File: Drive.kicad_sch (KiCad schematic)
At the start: 11 parts, among them Q1 EPC23104, U2 ACS711xEXLT-15AB

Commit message: Getting ready for fab
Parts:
- added C38, C39, C40, C41: 100n, 100V, 0603, X7R, Capacitor_SMD:C_0603_1608Metric, symbol Device:C
- added C54, C55, C56: 1u, 100V, 0805, X7R, Capacitor_SMD:C_0805_2012Metric, symbol Device:C
- C14: DigiKey (none) -> 490-GRM155Z71A105KE01JCT-ND
- C15, C16, C19: DigiKey (none) -> 490-10700-1-ND
- C18: DigiKey (none) -> 490-4762-1-ND
- R4, R5: DigiKey (none) -> 311-4.7JRCT-ND
- U2: LCSC (none) -> C150824
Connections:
- net GND: now also C38.2, C39.2, C40.2, C41.2, C54.2, C55.2, C56.2
- net Vdrive: now also C38.1, C39.1, C40.1, C41.1, C54.1, C55.1, C56.1

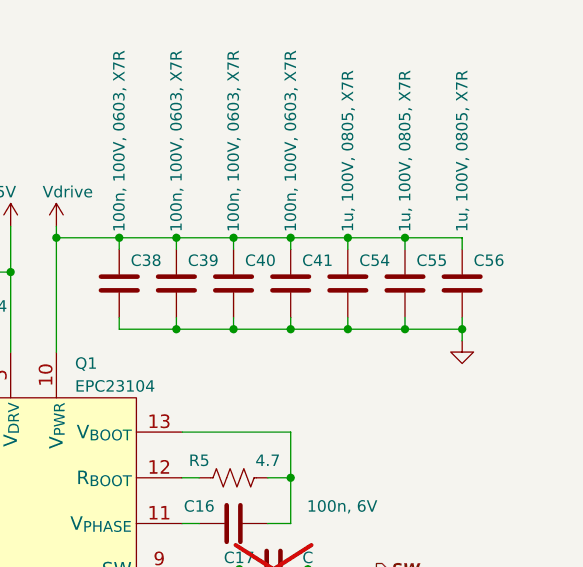
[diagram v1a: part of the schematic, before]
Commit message: Single-sided component placement
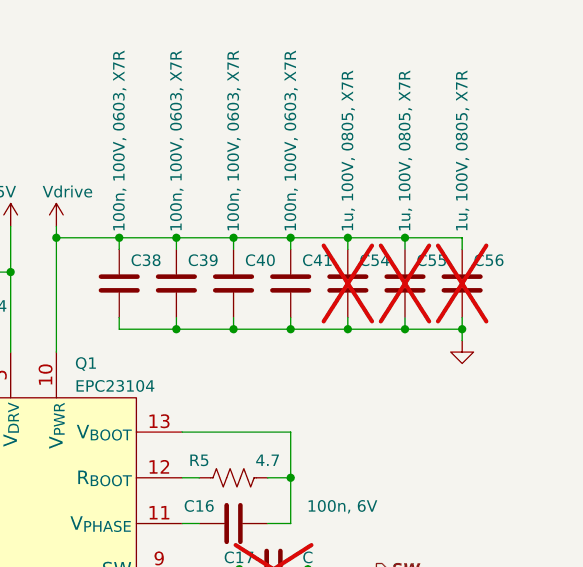
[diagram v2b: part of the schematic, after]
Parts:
- C54, C55, C56: now not fitted
- TP1: now left out of the parts list
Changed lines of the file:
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@@
   )
   (symbol (lib_id "Device:C") (at 168.275 63.5 0) (unit 1)
-    (in_bom yes) (on_board yes) (dnp no)
+    (in_bom yes) (on_board yes) (dnp yes)
     (property "Reference" "C55" (at 169.545 60.96 0)
       (effects (font (size 1.27 1.27)) (justify left))
@@
   )
   (symbol (lib_id "Device:C") (at 174.625 63.5 0) (unit 1)
-    (in_bom yes) (on_board yes) (dnp no)
+    (in_bom yes) (on_board yes) (dnp yes)
     (property "Reference" "C56" (at 175.895 60.96 0)
       (effects (font (size 1.27 1.27)) (justify left))
@@
   )
   (symbol (lib_id "Device:C") (at 161.925 63.5 0) (unit 1)
-    (in_bom yes) (on_board yes) (dnp no)
+    (in_bom yes) (on_board yes) (dnp yes)
     (property "Reference" "C54" (at 163.195 60.96 0)
       (effects (font (size 1.27 1.27)) (justify left))
@@
   )
   (symbol (lib_id "Connector:TestPoint") (at 154.94 123.825 180) (unit 1)
-    (in_bom yes) (on_board yes) (dnp no) (fields_autoplaced)
+    (in_bom no) (on_board yes) (dnp no) (fields_autoplaced)
     (property "Reference" "TP1" (at 157.48 126.492 0)
       (effects (font (size 1.27 1.27)) (justify right))

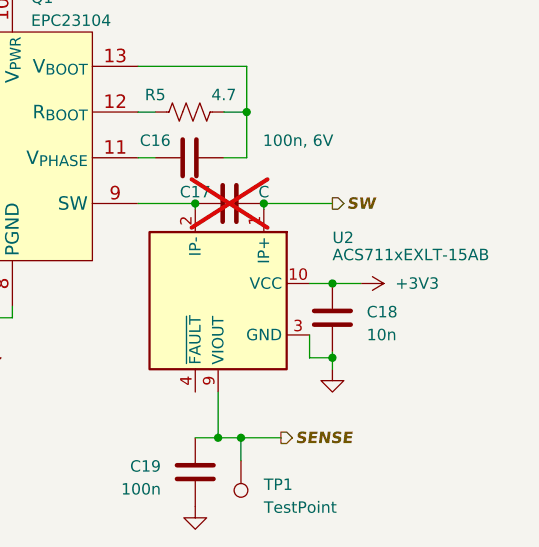
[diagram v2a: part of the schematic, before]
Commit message: Power supply and remove USB
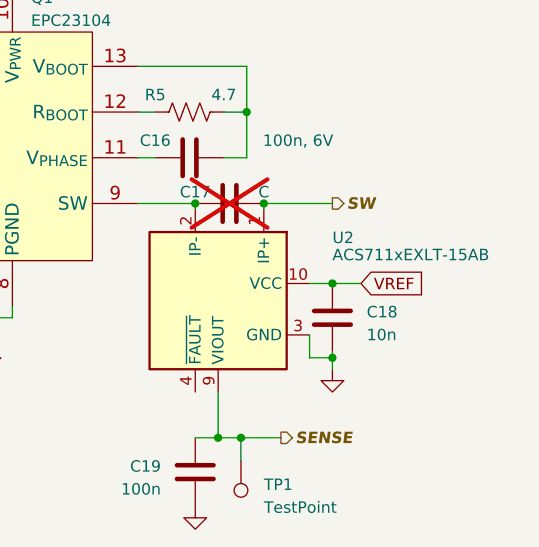
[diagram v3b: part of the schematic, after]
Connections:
- net +3V3 renamed VREF
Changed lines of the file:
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@@
     (stroke (width 0) (type default))
+  )
+  (global_label "VREF" (shape input) (at 168.275 104.14 0) (fields_autoplaced)
+    (effects (font (size 1.27 1.27)) (justify left))
+    (property "Intersheetrefs" "${INTERSHEET_REFS}" (at 175.777 104.14 0)
+      (effects (font (size 1.27 1.27)) (justify left) hide)
+    )
   )
   (hierarchical_label "SW" (shape output) (at 165.1 95.25 0) (fields_autoplaced)
@@
         )
       )
-    )
-  )
-  (symbol (lib_id "power:+3V3") (at 168.275 104.14 270) (mirror x) (unit 1)
-    (in_bom yes) (on_board yes) (dnp no)
-    (property "Reference" "#PWR038" (at 164.465 104.14 0)
-      (effects (font (size 1.27 1.27)) hide)
-    )
-    (property "Value" "+3V3" (at 172.085 104.14 90)
-      (effects (font (size 1.27 1.27)) (justify left))
-    )
-    (property "Footprint" "" (at 168.275 104.14 0)
-      (effects (font (size 1.27 1.27)) hide)
-    )
-    (property "Datasheet" "" (at 168.275 104.14 0)
-      (effects (font (size 1.27 1.27)) hide)
-    )
-    (pin "1")
-    (instances
-      (project "ECE4760 Motor Driver"
-        (path "/6b38a626-de8c-4b2d-bc76-3a02bc823a86/c589f15c-cfa0-468e-9e38-b6cac1cf329b"
-          (reference "#PWR038") (unit 1)
-        )
-        (path "/6b38a626-de8c-4b2d-bc76-3a02bc823a86/a080898b-4de6-4089-a4d2-49cdab3e2e2c"
-          (reference "#PWR048") (unit 1)
-        )
-        (path "/6b38a626-de8c-4b2d-bc76-3a02bc823a86/966e6479-76dc-4c15-80ee-30a40f91f040"
-          (reference "#PWR056") (unit 1)
-        )
-        (path "/6b38a626-de8c-4b2d-bc76-3a02bc823a86/7df790a7-70b3-4931-ac19-c23e231ae324"
-          (reference "#PWR064") (unit 1)
-        )
-      )

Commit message: Ready for design review
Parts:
- C16: renamed from C14; LCSC (none) -> C528974
- C17: renamed from C15; DigiKey 490-10700-1-ND -> 490-3261-1-ND; LCSC (none) -> C71629
- C18: renamed from C16; value 100n, 6V -> 100n; DigiKey 490-10700-1-ND -> 490-3261-1-ND; LCSC (none) -> C71629
- C20: renamed from C18; value 10n -> 1n; DigiKey 490-4762-1-ND -> 490-GCM155R71H102KA37JCT-ND; LCSC (none) -> C1852263
- C21: renamed from C19; DigiKey 490-10700-1-ND -> 490-3261-1-ND; LCSC (none) -> C71629
- C?: renamed from C40; DigiKey 490-3285-1-ND -> 490-13420-1-ND; LCSC (none) -> C161117
- C?: renamed from C55; LCSC (none) -> C5370002
- C?: renamed from C56; LCSC (none) -> C5370002
- C?: renamed from C38; DigiKey 490-3285-1-ND -> 490-13420-1-ND; LCSC (none) -> C161117
- C?: renamed from C54; LCSC (none) -> C5370002
- C?: renamed from C39; DigiKey 490-3285-1-ND -> 490-13420-1-ND; LCSC (none) -> C161117
- C?: renamed from C41; DigiKey 490-3285-1-ND -> 490-13420-1-ND; LCSC (none) -> C161117
- R4, R5: LCSC (none) -> C137862
- TP3: renamed from TP1; value TestPoint -> Sense
- renumbered C17 to C19
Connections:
- net VREF renamed +3V3

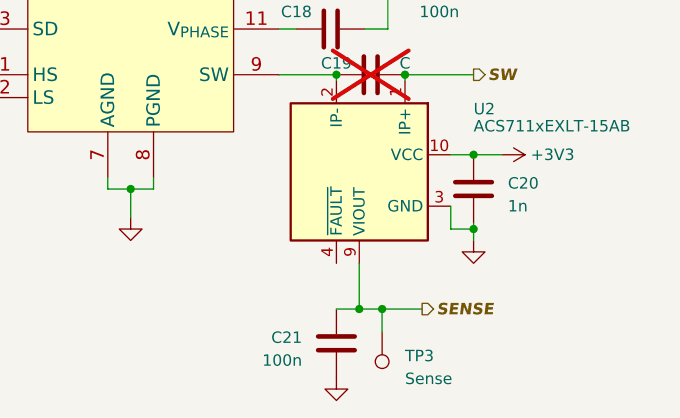
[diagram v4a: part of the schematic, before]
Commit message: Tweaking pin assignments
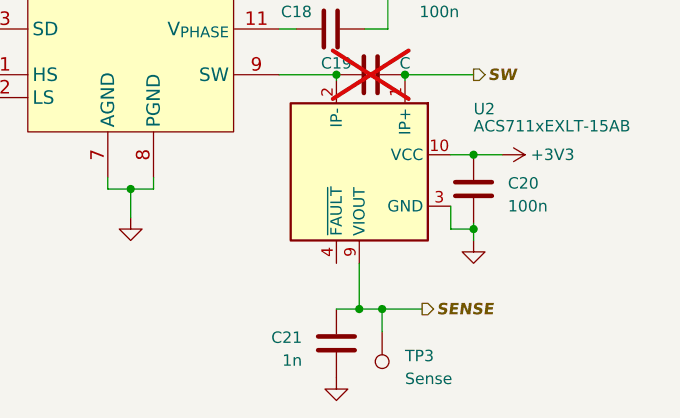
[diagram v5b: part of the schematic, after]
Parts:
- C20: value 1n -> 100n
- C21: value 100n -> 1n
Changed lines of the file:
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@@
       (effects (font (size 1.27 1.27)) (justify right))
     )
-    (property "Value" "1n" (at 168.91 109.855 0)
+    (property "Value" "100n" (at 168.91 109.855 0)
       (effects (font (size 1.27 1.27)) (justify right))
     )
@@
       (effects (font (size 1.27 1.27)) (justify right))
     )
-    (property "Value" "100n" (at 146.05 127 0)
+    (property "Value" "1n" (at 146.05 127 0)
       (effects (font (size 1.27 1.27)) (justify right))
     )

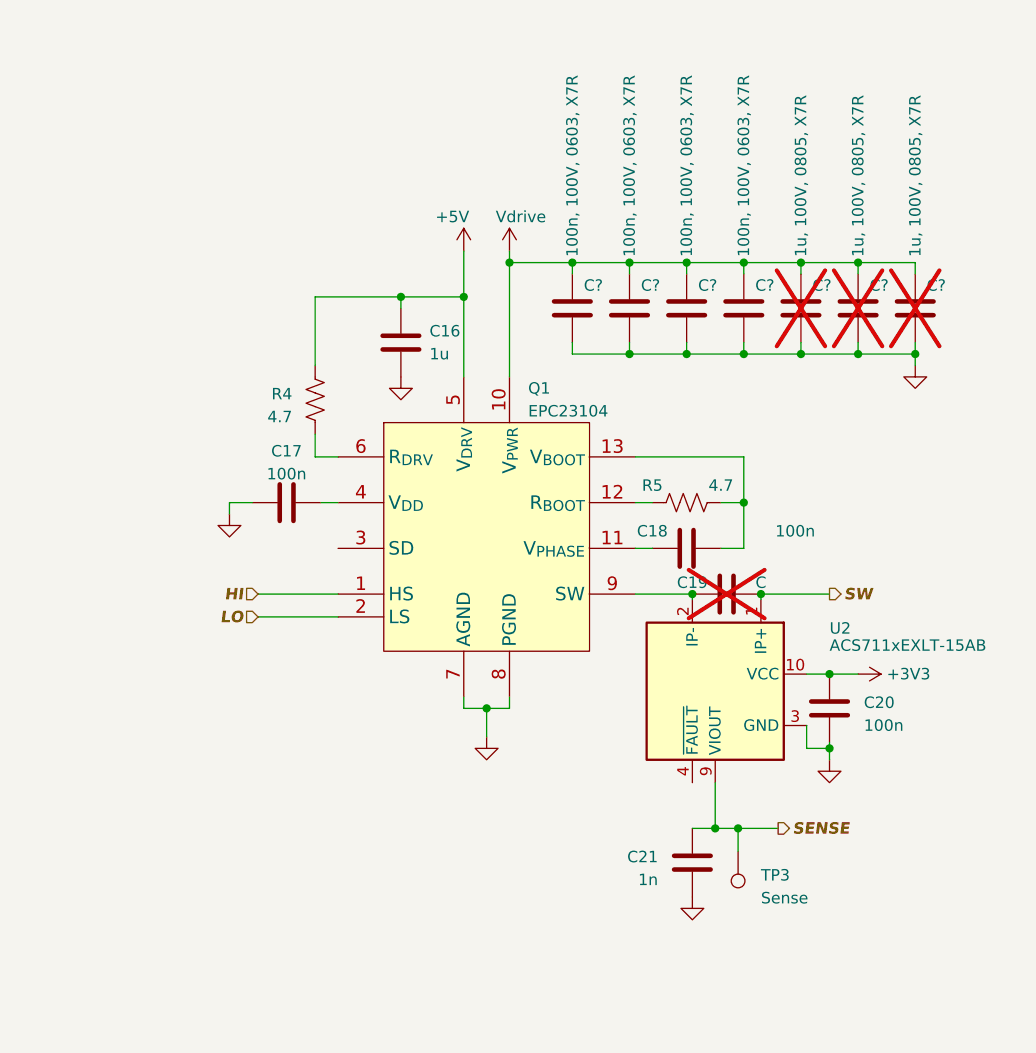
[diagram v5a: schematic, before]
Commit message: Change MCU package and MOSFETs
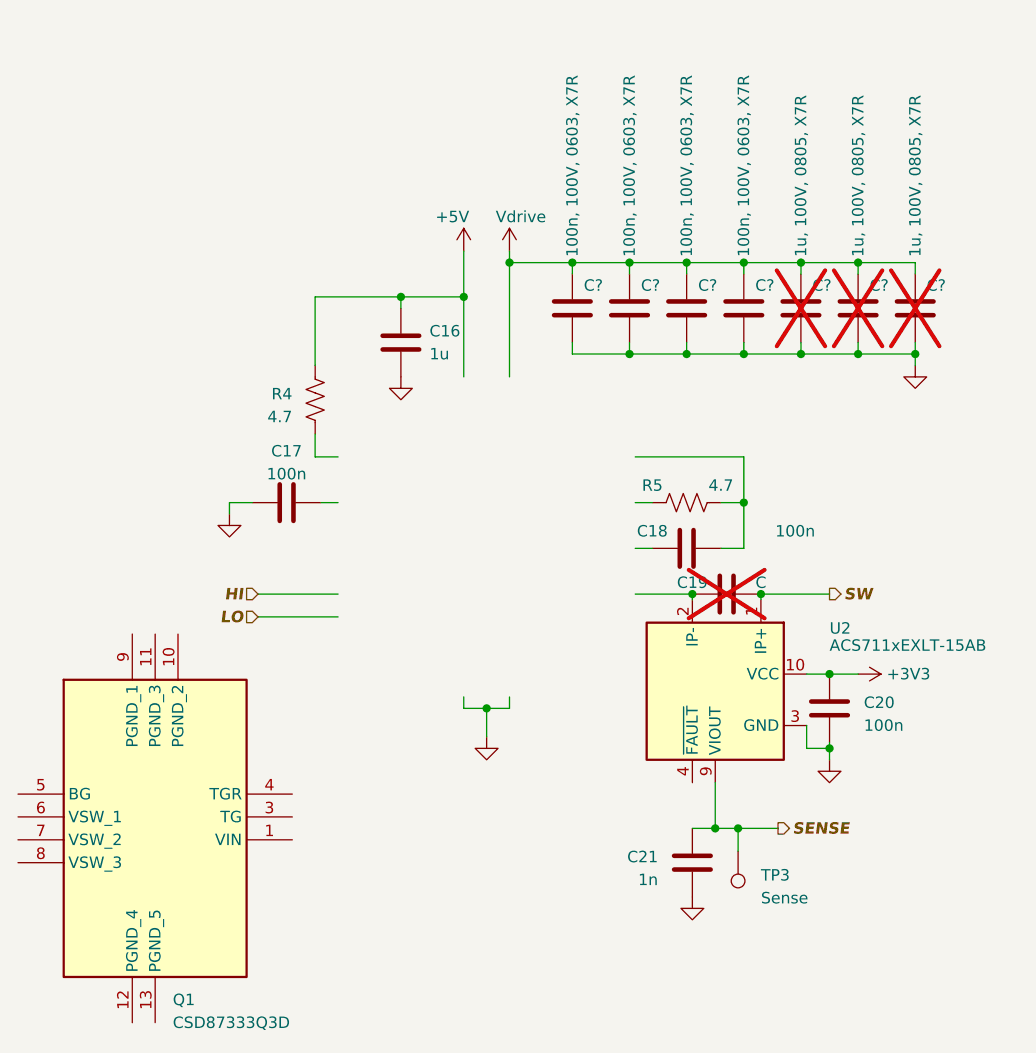
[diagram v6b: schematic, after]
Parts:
- removed Q1: EPC23104, EPC:EPC2310x, symbol EPC:EPC23104
- added Q1: CSD87333Q3D, CSD87333Q3D:CSD87333Q3D, symbol CSD87333Q3D:CSD87333Q3D

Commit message: Update
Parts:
- removed C17: 100n, Capacitor_SMD:C_0402_1005Metric, symbol Device:C
- removed C? (x3): 100n, 100V, 0603, X7R, Capacitor_SMD:C_0603_1608Metric, symbol Device:C
- removed C? (x3): 1u, 100V, 0805, X7R, Capacitor_SMD:C_0805_2012Metric, symbol Device:C
- added U11: DGD05473FNQ, Package_DFN_QFN:DFN-10-1EP_3x3mm_P0.5mm_EP1.65x2.38mm, symbol Driver_FET:IR2106
- C16: value 1u -> 100n
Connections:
- net GND is gone; now on net EP: C16.2, C20.1, C21.1, C?.2, U2.3 (GND)
- net +5V: now also U11.1 (VCC); no longer R4.1
- net HI: now also U11.7 (HIN)
- net LO: now also U11.8 (LIN)
- net Vdrive: now also Q1.1 (VIN)
- net at R5.1: now also U11.10 (LO)
- net at R5.2: now also Q1.5 (BG); no longer C18.2
- net EP: now reaches Q1.10 (GND)
- net EP: now also Q1.11 (GND), Q1.12 (GND), Q1.13 (GND), Q1.9 (GND), U11.11 (EP), U11.9 (COM)
- net at Q1.3 (TG): now also R4.1
- net at Q1.4 (TGR): now also C18.2, U11.5 (VS)
- net at Q1.6 (SW): now also C19.1, Q1.7 (SW), Q1.8 (SW), U2.2 (IP-)
- net at C18.1: now also U11.3 (VB)
- net at R4.2: now also U11.4 (HO)
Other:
- moved on the sheet: C16, C18, C?, R4, R5

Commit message: Boards ordered!
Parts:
- added C?: 4u7, 50V, 0805, X7R, Capacitor_SMD:C_0805_2012Metric, symbol Device:C
- C15: renamed from C16; DigiKey 490-GRM155Z71A105KE01JCT-ND -> 490-3261-1-ND; LCSC C528974 -> C71629
- C20: DigiKey 490-GCM155R71H102KA37JCT-ND -> 490-3261-1-ND; LCSC C1852263 -> C71629
- C21: DigiKey 490-3261-1-ND -> 490-GCM155R71H102KA37JCT-ND; LCSC C71629 -> C277522
- C?: value 100n, 100V, 0603, X7R -> 100n, 50V, 0603, X7R
- Q1: LCSC (none) -> C90396
- R5: renamed from R4; value 4.7 -> 4R7
- R6: renamed from R5; value 4.7 -> 4R7
- renumbered TP3 to TP2, U2 to U6, U11 to U9
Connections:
- net EP: now also C?.2
- net Vdrive: now also C?.1
- net Fault_Enable: now reaches U9.6 (EN)
- net Fault_Enable: now also U6.4 (~{FAULT})
